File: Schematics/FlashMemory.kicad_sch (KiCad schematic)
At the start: 4 parts, among them U8 W25Q128JVP

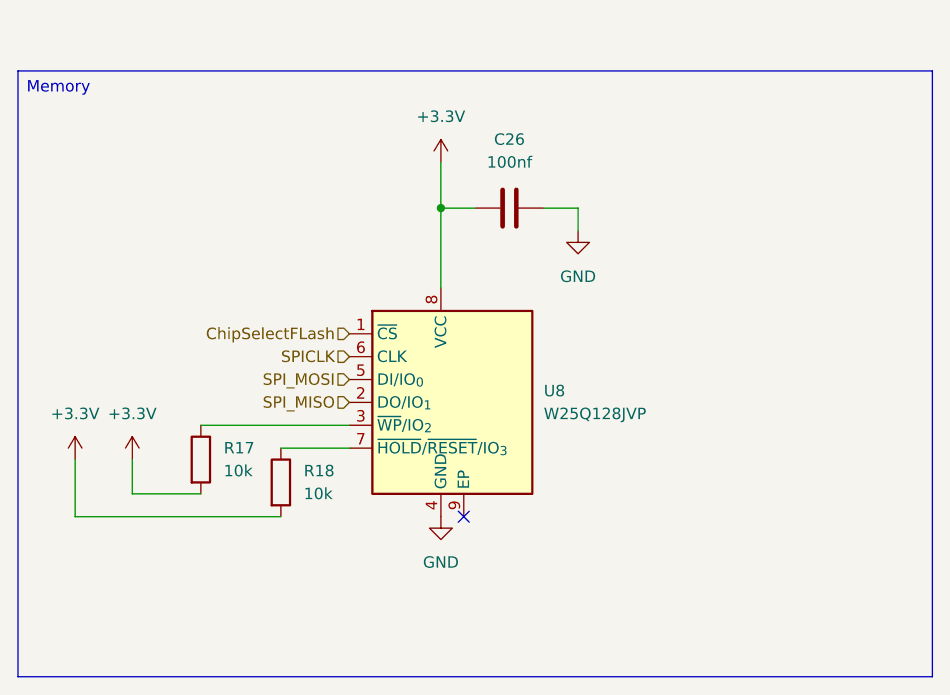
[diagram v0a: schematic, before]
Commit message: added aux pyro added reverse polarity protection re routed just need to clean up and check pin assignments
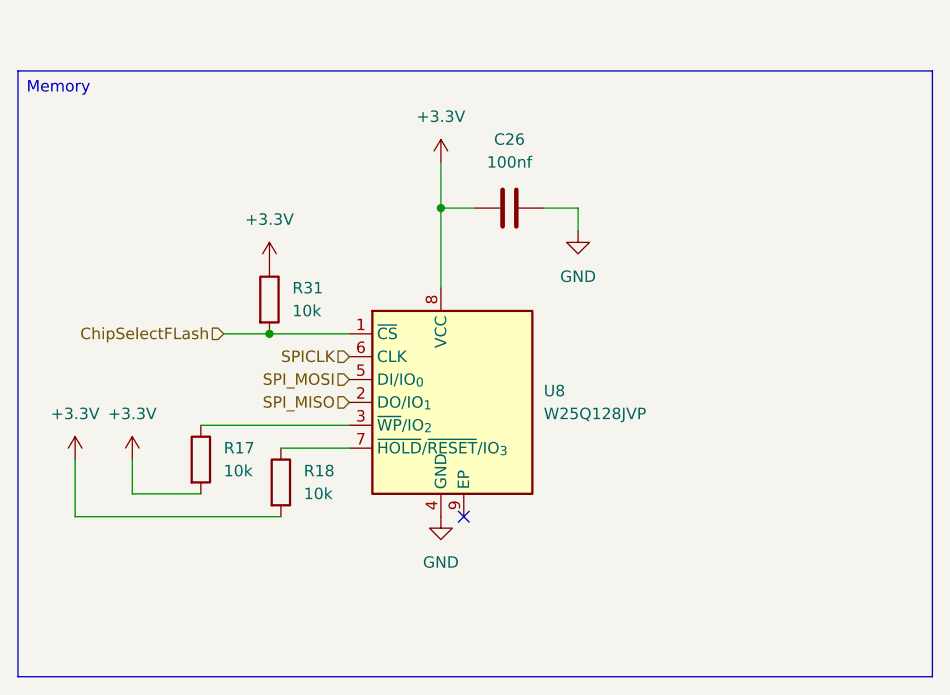
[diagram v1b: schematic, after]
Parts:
- added R31: 10k, Resistor_SMD:R_0805_2012Metric_Pad1.20x1.40mm_HandSolder, symbol Device:R
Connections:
- net +3.3V: now also R31.1
- net ChipSelectFLash: now also R31.2

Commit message: added comments, awaiting review
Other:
- note added: "Redundant storage to be used in tandem with SD card"
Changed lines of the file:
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@@
 	(generator_version "9.0")
 	(paper "A4")
+	(text "Redundant storage to be used in tandem with SD card"
+		(exclude_from_sim no)
+		(at 126.746 43.942 0)
+		(effects
+			(font
+				(size 1.27 1.27)
+			)
+		)
+	)
 	(text_box "Memory\n"
 		(exclude_from_sim no)

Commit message: updated to KiCad 10.0, updated .gitignore
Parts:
- R17, R18, R31: LCSC C84376 -> C17414
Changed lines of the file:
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@@
 			)
 		)
-		(property "LCSC" "C84376"
+		(property "LCSC" "C17414"
 			(at 109.22 93.98 0)
 			(effects
@@
 			)
 		)
-		(property "LCSC" "C84376"
+		(property "LCSC" "C17414"
 			(at 107.95 73.66 0)
 			(effects
@@
 			)
 		)
-		(property "LCSC" "C84376"
+		(property "LCSC" "C17414"
 			(at 100.33 91.44 0)
 			(effects
